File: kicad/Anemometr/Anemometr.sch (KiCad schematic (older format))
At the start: 157 parts, among them J10 +Z3, J11 -Z3, J12 +Z4, J13 -Z4, J14 SWD, J15 SWC, J16 Z4, J17 Z4, J18 1 TxD+, J19 2 TxD-, J2 Conn_01x01_Female, J20 3 RxD+, J21 4, J22 5, J23 6 RxD-, J24 7, J25 8, J26 Z4, J27 Z4, J28 Z4, J29 Z4, J3 RST, J30 Z4, J31 Z4, J32 Z4, J33 Z4, J34 Z4, J35 Z4, J4 TxD, J5 RxD, J6 +Z1, J7 -Z1, J8 +Z2, J9 -Z2, U1 TS5A3166DBVR, U10 MCP1700-3002E, U2 LMV7239, U3 TS5A3166DBVR, U4 TS5A3166DBVR, U5 STM32F103C8Tx, U6 TS5A3166DBVR, U7 LM2734Y, U8 MCP1700-5002E, U9 MCP1700-3002E, Y1 8MHz, Y2 25MHz

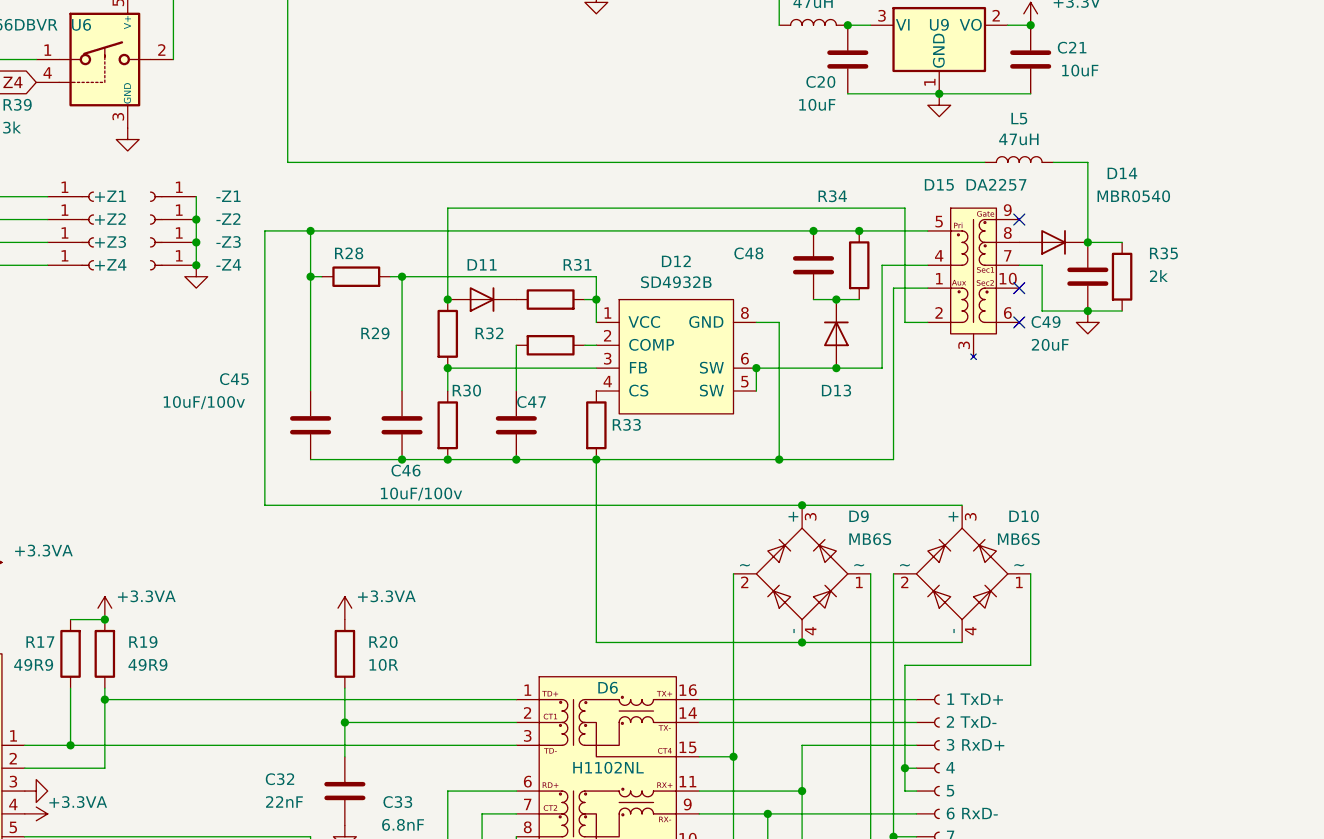
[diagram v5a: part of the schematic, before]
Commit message: изменено:      kicad/Anemometr/Anemometr-cache.lib 	изменено:      kicad/Anemometr/Anemometr.kicad_pcb 	изменено:      kicad/Anemometr/Anemometr.kicad_pcb-bak 	изменено:      kicad/Anemometr/Anemometr.sch 	изменено:      kicad/Anemometr/Anemometr.sch-bak 	изменено:      kicad/Anemometr/fp-info-cache
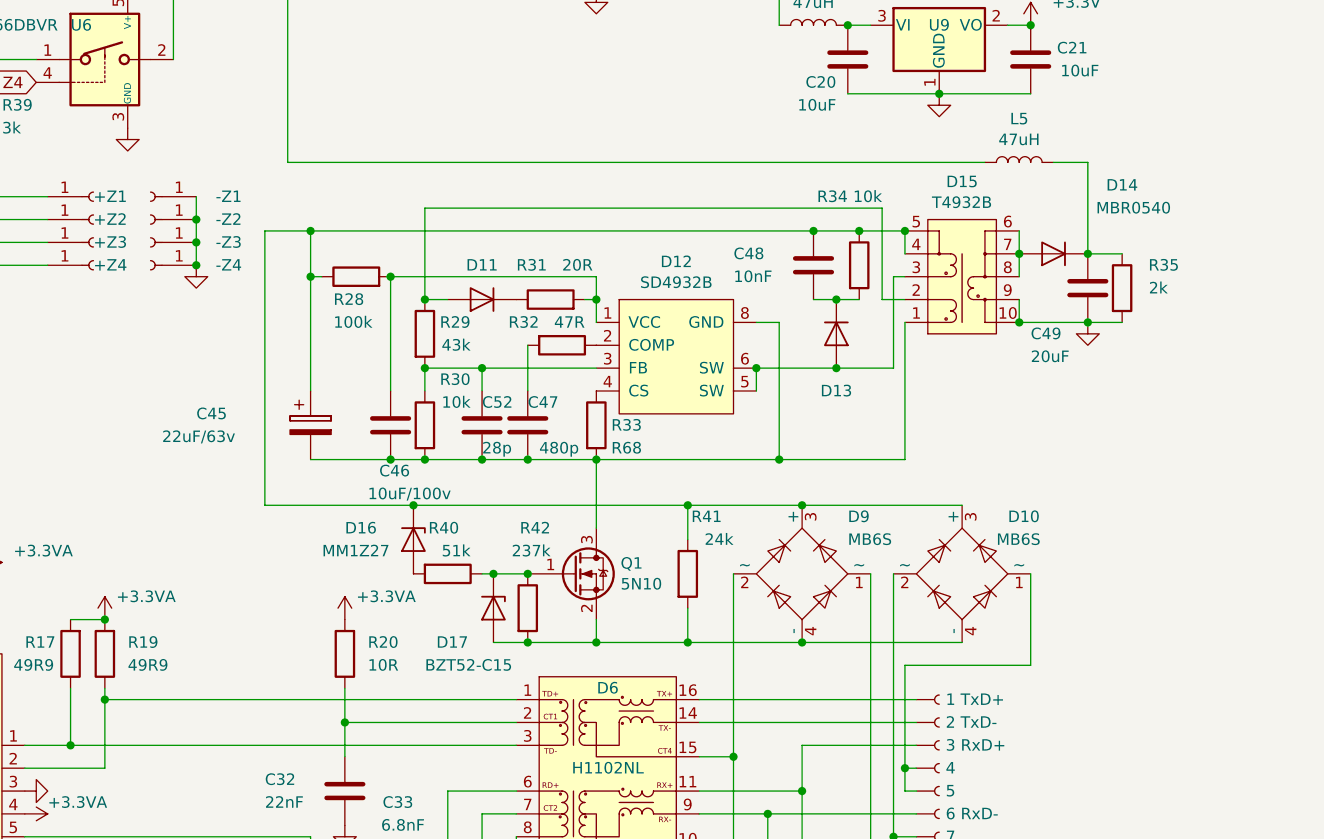
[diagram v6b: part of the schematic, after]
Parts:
- removed C45: 10uF/100v, Capacitor_SMD:C_0805_2012Metric, symbol Device:C
- removed D15: DA2257, My-library:DA2257, symbol Anemometr-rescue:DA2257-My_Library
- added C45: 22uF/63v, Capacitor_SMD:CP_Elec_6.3x7.7, symbol Device:CP
- added C52: 28p, Capacitor_SMD:C_0603_1608Metric, symbol Device:C
- added D15: T4932B, My-library:DA2257, symbol My_Library:T4932B
- added D16: MM1Z27, Diode_SMD:D_SOD-123, symbol Device:D_Zener
- added D17: BZT52-C15, Diode_SMD:D_SOD-123, symbol Device:D_Zener
- added Q1: 5N10, Package_TO_SOT_SMD:SOT-23, symbol Device:Q_NMOS_GSD
- added R40: 51k, Resistor_SMD:R_0603_1608Metric, symbol Device:R
- added R41: 24k, Resistor_SMD:R_0603_1608Metric, symbol Device:R
- added R42: 237k, Resistor_SMD:R_0603_1608Metric, symbol Device:R
- C47: value 6.8nF -> 480p
- C48: value 6.8nF -> 10nF
- R28: value 150R -> 100k
- R29: value 150R -> 43k
- R30, R34: value 150R -> 10k
- R31: value 150R -> 20R
- R32: value 150R -> 47R
- R33: value 150R -> R68
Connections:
- net GND: now also D15.10, D15.9
- net at C46.2, C47.2, D12.8 (GND)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: now also C45.2, C52.2, D15.1, Q1.3 (D); no longer D10.4 (-), D9.4 (-)
- net at D11.2 (A), R29.1: now also D15.2
- net at D12.5 (SW), D12.6 (SW), D13.2 (A): now also D15.3
- net at C48.1, D10.3 (+), D9.3 (+)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: now also C45.1, D15.4, D15.5, D16.1 (K), R41.1
- net at D14.2 (A): now also D15.6, D15.7, D15.8
- net at D12.3 (FB), R29.2, R30.1: now also C52.1
- new net: D17.1 (K), Q1.1 (G), R40.1, R42.1
- new net: D10.4 (-), D17.2 (A), D9.4 (-), Q1.2 (S), R41.2, R42.2
- new net: D16.2 (A), R40.2
- no-connect marks 32 -> 29
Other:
- moved on the sheet: C46, C47, C49, D14, R29, R30, R32, R35

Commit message: изменено:      kicad/Anemometr/Anemometr.kicad_pcb 	изменено:      kicad/Anemometr/Anemometr.kicad_pcb-bak 	изменено:      kicad/Anemometr/Anemometr.sch 	изменено:      kicad/Anemometr/Anemometr.sch-bak 	изменено:      kicad/Anemometr/fp-info-cache
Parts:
- removed C49: 20uF, Capacitor_SMD:C_1210_3225Metric, symbol Device:C
- removed R22: 75R, Resistor_SMD:R_0402_1005Metric, symbol Device:R
- added C49: 220uF, Capacitor_Tantalum_SMD:CP_EIA-7343-15_Kemet-W, symbol Device:CP
- added D18, D19: LED, LED_SMD:LED_0603_1608Metric, symbol Device:LED
- added J1: +5.5v, My-library:SMD-CONN, symbol Connector:Conn_01x01_Female
- added R43: 4.7k, Resistor_SMD:R_0603_1608Metric, symbol Device:R
- added R44: 2k, Resistor_SMD:R_0603_1608Metric, symbol Device:R
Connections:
- net GND: now also C49.2, D18.1 (K), D19.1 (K)
- net at C22.2, D2.2 (A), L5.1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: now also R43.2
- net at C17.2, L1.2, L2.1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: now also J1.1 (Pin_1), R44.1
- net at D6.11, J20.1: now also R23.2; no longer R24.2
- net at D6.9, J23.1: now also R24.2; no longer R23.2
- net at Q1.1 (G), R40.1, R42.1: now also D17.2 (A); no longer D17.1 (K)
- net at D10.4 (-), D9.4 (-), Q1.2 (S)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: now also D17.1 (K); no longer D17.2 (A)
- net at D14.1 (K), L5.2, R35.1: now also C49.1
- new net: D18.2 (A), R43.1
- new net: D19.2 (A), R44.2
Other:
- moved on the sheet: R23, R24, R41
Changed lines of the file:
@@
 U 1 1 61DA4E2B
 P 9900 3800
-F 0 "R12" V 10200 3800 50  0000 R CNN
-F 1 "100k" V 10100 3800 50  0000 R CNN
+F 0 "R12" V 10200 3600 50  0000 R CNN
+F 1 "100k" V 10100 3600 50  0000 R CNN
 F 2 "Resistor_SMD:R_0805_2012Metric" V 9830 3800 50  0001 C CNN
 F 3 "~" H 9900 3800 50  0001 C CNN
@@
 $EndComp
 $Comp
-L Device:R R21
-U 1 1 61FFF702
-P 9950 8100
-F 0 "R21" H 10150 8050 50  0000 R CNN
-F 1 "75R" H 10150 8150 50  0000 R CNN
-F 2 "Resistor_SMD:R_0402_1005Metric" V 9880 8100 50  0001 C CNN
-F 3 "~" H 9950 8100 50  0001 C CNN
-	1    9950 8100
-	-1   0    0    1
-$EndComp
-$Comp
-L Device:R R22
-U 1 1 61FFFDD0
-P 10100 8100
-F 0 "R22" H 10100 8450 50  0000 R CNN
-F 1 "75R" H 10100 8550 50  0000 R CNN
-F 2 "Resistor_SMD:R_0402_1005Metric" V 10030 8100 50  0001 C CNN
-F 3 "~" H 10100 8100 50  0001 C CNN
-	1    10100 8100
-	-1   0    0    1
-$EndComp
-$Comp
-L Device:C C35
-U 1 1 62000309
-P 9950 8400
-F 0 "C35" H 10150 8350 50  0000 L CNN
-F 1 "4.7nF/2kV" H 10100 8450 50  0000 L CNN
-F 2 "Capacitor_SMD:C_0805_2012Metric" H 9988 8250 50  0001 C CNN
-F 3 "~" H 9950 8400 50  0001 C CNN
-	1    9950 8400
-	-1   0    0    1
-$EndComp
-$Comp
-L power:GND #PWR048
-U 1 1 6200A94F
-P 9950 8550
-F 0 "#PWR048" H 9950 8300 50  0001 C CNN
-F 1 "GND" H 9955 8377 50  0001 C CNN
-F 2 "" H 9950 8550 50  0001 C CNN
-F 3 "" H 9950 8550 50  0001 C CNN
-	1    9950 8550
-	1    0    0    -1
-$EndComp
-$Comp
 L Anemometr-rescue:Conn-My_Library J18
 U 1 1 6201FB36
@@
 	9950 7350 10900 7350
 Wire Wire Line
-	9950 7650 10400 7650
-Wire Wire Line
-	9950 7500 10100 7500
-$Comp
-L Device:R R23
-U 1 1 62116815
-P 10250 8100
-F 0 "R23" H 10200 8450 50  0000 R CNN
-F 1 "150R" H 10200 8550 50  0000 R CNN
-F 2 "Resistor_SMD:R_0402_1005Metric" V 10180 8100 50  0001 C CNN
-F 3 "~" H 10250 8100 50  0001 C CNN
-	1    10250 8100
-	-1   0    0    1
-$EndComp
-$Comp
-L Device:R R24
-U 1 1 6211700D
-P 10400 8100
-F 0 "R24" H 10300 8050 50  0000 R CNN
-F 1 "150R" H 10300 8150 50  0000 R CNN
-F 2 "Resistor_SMD:R_0402_1005Metric" V 10330 8100 50  0001 C CNN
-F 3 "~" H 10400 8100 50  0001 C CNN
-	1    10400 8100
-	-1   0    0    1
-$EndComp
-Wire Wire Line
-	10400 7650 10400 7450
-Wire Wire Line
-	10400 7450 10900 7450
+	9950 7650 10100 7650
 $Comp
 L Device:LED D8
@@
 Connection ~ 10800 7850
 Wire Wire Line
-	10100 7500 10100 6700
-Wire Wire Line
 	10700 6700 10700 7900
 Wire Wire Line
@@
 $EndComp
 $Comp
-L Device:C C49
-U 1 1 629FDA3F
-P 11650 5450
-F 0 "C49" H 11400 5250 50  0000 L CNN
-F 1 "20uF" H 11400 5150 50  0000 L CNN
-F 2 "Capacitor_SMD:C_1210_3225Metric" H 11688 5300 50  0001 C CNN
-F 3 "~" H 11650 5450 50  0001 C CNN
-	1    11650 5450
-	1    0    0    -1
-$EndComp
-$Comp
 L Device:R R35
 U 1 1 629FDF7E
@@
 	9700 1800 9700 2000
 Wire Wire Line
-	9950 7950 9950 7900
-Connection ~ 9950 7900
-Wire Wire Line
-	10100 7950 10100 7500
-Connection ~ 10100 7500
-Wire Wire Line
-	9950 7750 10250 7750
-Wire Wire Line
-	10250 7950 10250 7750
-Connection ~ 10250 7750
-Wire Wire Line
-	10250 7750 10900 7750
-Wire Wire Line
-	10400 7950 10400 7650
-Connection ~ 10400 7650
-Wire Wire Line
-	9950 8250 10100 8250
-Connection ~ 9950 8250
-Connection ~ 10100 8250
-Wire Wire Line
-	10100 8250 10250 8250
-Connection ~ 10250 8250
-Wire Wire Line
-	10250 8250 10400 8250
-Wire Wire Line
 	8750 5900 8750 5800
 Wire Wire Line
-	9500 7000 9900 7000
+	9500 7000 9700 7000
 Wire Wire Line
 	8150 4900 11200 4900
@@
 	8150 3150 8550 3150
 Wire Wire Line
-	8150 3150 8150 4900
+	8150 3150 8150 4300
 Connection ~ 8550 3150
 $Comp
@@
 U 1 1 61F86A88
 P 9400 6700
-F 0 "Q1" H 9606 6746 50  0000 L CNN
-F 1 "5N10" H 9606 6655 50  0000 L CNN
+F 0 "Q1" H 9450 6350 50  0000 L CNN
+F 1 "5N10" H 9600 6350 50  0000 L CNN
 F 2 "Package_TO_SOT_SMD:SOT-23" H 9600 6800 50  0001 C CNN
 F 3 "~" H 9400 6700 50  0001 C CNN
@@
 L Device:R R41
 U 1 1 6207208D
-P 9900 6700
-F 0 "R41" H 10050 6950 50  0000 R CNN
-F 1 "24k" H 10100 6850 50  0000 R CNN
-F 2 "Resistor_SMD:R_0603_1608Metric" V 9830 6700 50  0001 C CNN
-F 3 "~" H 9900 6700 50  0001 C CNN
-	1    9900 6700
-	1    0    0    -1
-$EndComp
-Wire Wire Line
-	9900 6550 9900 6400
-Connection ~ 9900 6400
-Wire Wire Line
-	9900 6400 10400 6400
-Wire Wire Line
-	9900 6850 9900 7000
-Connection ~ 9900 7000
-Wire Wire Line
-	9900 7000 10400 7000
+P 9700 6700
+F 0 "R41" H 9850 6950 50  0000 R CNN
+F 1 "24k" H 9900 6850 50  0000 R CNN
+F 2 "Resistor_SMD:R_0603_1608Metric" V 9630 6700 50  0001 C CNN
+F 3 "~" H 9700 6700 50  0001 C CNN
+	1    9700 6700
+	1    0    0    -1
+$EndComp
 $Comp
 L Device:D_Zener D16
@@
 Connection ~ 8700 6400
 Wire Wire Line
-	8700 6400 9900 6400
+	8700 6400 9700 6400
 Wire Wire Line
 	9000 6700 9050 6700
@@
 U 1 1 620B088D
 P 9050 6850
-F 0 "D17" V 9200 6600 50  0000 L CNN
-F 1 "BZT52-C15" V 9300 6550 50  0000 L CNN
+F 0 "D17" V 8950 6900 50  0000 L CNN
+F 1 "BZT52-C15" V 8850 6750 50  0000 L CNN
 F 2 "Diode_SMD:D_SOD-123" H 9050 6850 50  0001 C CNN
 F 3 "~" H 9050 6850 50  0001 C CNN
 	1    9050 6850
-	0    1    1    0
+	0    -1   -1   0
 $EndComp
 Connection ~ 9050 6700
@@
 	10800 5400 10850 5400
 Wire Wire Line
-	10850 5600 10850 6200
-Wire Wire Line
 	10300 6200 10850 6200
 Wire Wire Line
@@
 Wire Wire Line
 	11650 4900 11650 5300
+$Comp
+L Device:R R43
+U 1 1 620F34A0
+P 8300 4300
+F 0 "R43" V 8100 4350 50  0000 R CNN
+F 1 "4.7k" V 8200 4350 50  0000 R CNN
+F 2 "Resistor_SMD:R_0603_1608Metric" V 8230 4300 50  0001 C CNN
+F 3 "~" H 8300 4300 50  0001 C CNN
+	1    8300 4300
+	0    1    1    0
+$EndComp
+Connection ~ 8150 4300
+Wire Wire Line
+	8150 4300 8150 4900
+$Comp
+L Device:LED D18
+U 1 1 620F6B14
+P 8450 4450
+F 0 "D18" V 8550 4300 50  0000 R CNN
+F 1 "LED" V 8398 4333 50  0001 R CNN
+F 2 "LED_SMD:LED_0603_1608Metric" H 8450 4450 50  0001 C CNN
+F 3 "~" H 8450 4450 50  0001 C CNN
+	1    8450 4450
+	0    -1   -1   0
+$EndComp
+$Comp
+L power:GND #PWR052
+U 1 1 620FBFC5
+P 8450 4600
+F 0 "#PWR052" H 8450 4350 50  0001 C CNN
+F 1 "GND" H 8455 4427 50  0001 C CNN
+F 2 "" H 8450 4600 50  0001 C CNN
+F 3 "" H 8450 4600 50  0001 C CNN
+	1    8450 4600
+	1    0    0    -1
+$EndComp
+$Comp
+L Connector:Conn_01x01_Female J1
+U 1 1 62105095
+P 10300 2900
+F 0 "J1" H 9800 2900 50  0001 C CNN
+F 1 "+5.5v" V 10400 2800 50  0000 L CNN
+F 2 "My-library:SMD-CONN" H 10300 2900 50  0001 C CNN
+F 3 "~" H 10300 2900 50  0001 C CNN
+	1    10300 2900
+	0    -1   -1   0
+$EndComp
+$Comp
+L Device:R R44
+U 1 1 621C9B5C
+P 10150 3100
+F 0 "R44" V 9950 3150 50  0000 R CNN
+F 1 "2k" V 10050 3150 50  0000 R CNN
+F 2 "Resistor_SMD:R_0603_1608Metric" V 10080 3100 50  0001 C CNN
+F 3 "~" H 10150 3100 50  0001 C CNN
+	1    10150 3100
+	0    1    1    0
+$EndComp
+$Comp
+L Device:LED D19
+U 1 1 621CB231
+P 10000 3250
+F 0 "D19" V 10000 3150 50  0000 R CNN
+F 1 "LED" V 9948 3133 50  0001 R CNN
+F 2 "LED_SMD:LED_0603_1608Metric" H 10000 3250 50  0001 C CNN
+F 3 "~" H 10000 3250 50  0001 C CNN
+	1    10000 3250
+	0    -1   -1   0
+$EndComp
+Connection ~ 10300 3100
+$Comp
+L power:GND #PWR061
+U 1 1 6225054D
+P 10000 3400
+F 0 "#PWR061" H 10000 3150 50  0001 C CNN
+F 1 "GND" H 10005 3227 50  0001 C CNN
+F 2 "" H 10000 3400 50  0001 C CNN
+F 3 "" H 10000 3400 50  0001 C CNN
+	1    10000 3400
+	1    0    0    -1
+$EndComp
+$Comp
+L Device:CP C49
+U 1 1 62482746
+P 11650 5450
+F 0 "C49" H 11350 5200 50  0000 L CNN
+F 1 "220uF" H 11350 5100 50  0000 L CNN
+F 2 "Capacitor_Tantalum_SMD:CP_EIA-7343-15_Kemet-W" H 11688 5300 50  0001 C CNN
+F 3 "~" H 11650 5450 50  0001 C CNN
+	1    11650 5450
+	1    0    0    -1
+$EndComp
+Wire Wire Line
+	9700 6850 9700 7000
+Connection ~ 9700 7000
+Wire Wire Line
+	9700 6550 9700 6400
+Connection ~ 9700 6400
+Wire Wire Line
+	9700 6400 10400 6400
+Wire Wire Line
+	9700 7000 10400 7000
+Wire Wire Line
+	9950 7500 10000 7500
+Wire Wire Line
+	10000 7500 10000 6700
+Wire Wire Line
+	10000 6700 10100 6700
+Wire Wire Line
+	10100 7650 10100 7450
+Wire Wire Line
+	10100 7450 10900 7450
+Wire Wire Line
+	10850 5600 10850 6200
+$Comp
+L power:GND #PWR048
+U 1 1 6200A94F
+P 9950 8550
+F 0 "#PWR048" H 9950 8300 50  0001 C CNN
+F 1 "GND" H 9955 8377 50  0001 C CNN
+F 2 "" H 9950 8550 50  0001 C CNN
+F 3 "" H 9950 8550 50  0001 C CNN
+	1    9950 8550
+	1    0    0    -1
+$EndComp
+$Comp
+L Device:C C35
+U 1 1 62000309
+P 9950 8400
+F 0 "C35" H 10150 8350 50  0000 L CNN
+F 1 "4.7nF/2kV" H 10100 8450 50  0000 L CNN
+F 2 "Capacitor_SMD:C_0805_2012Metric" H 9988 8250 50  0001 C CNN
+F 3 "~" H 9950 8400 50  0001 C CNN
+	1    9950 8400
+	-1   0    0    1
+$EndComp
+Wire Wire Line
+	10250 7750 10900 7750
+Wire Wire Line
+	9950 7750 10250 7750
+Connection ~ 10250 7750
+Wire Wire Line
+	10250 7950 10250 7750
+Connection ~ 9950 7900
+Wire Wire Line
+	9950 7950 9950 7900
+Connection ~ 10100 7650
+Wire Wire Line
+	10100 7950 10100 7650
+Connection ~ 9950 8250
+$Comp
+L Device:R R21
+U 1 1 61FFF702
+P 9950 8100
+F 0 "R21" H 10150 8050 50  0000 R CNN
+F 1 "75R" H 10150 8150 50  0000 R CNN
+F 2 "Resistor_SMD:R_0402_1005Metric" V 9880 8100 50  0001 C CNN
+F 3 "~" H 9950 8100 50  0001 C CNN
+	1    9950 8100
+	-1   0    0    1
+$EndComp
+Wire Wire Line
+	10100 8250 10250 8250
+Wire Wire Line
+	9950 8250 10100 8250
+Connection ~ 10100 8250
+$Comp
+L Device:R R23
+U 1 1 62116815
+P 10100 8100
+F 0 "R23" H 10050 8450 50  0000 R CNN
+F 1 "150R" H 10050 8550 50  0000 R CNN
+F 2 "Resistor_SMD:R_0402_1005Metric" V 10030 8100 50  0001 C CNN
+F 3 "~" H 10100 8100 50  0001 C CNN
+	1    10100 8100
+	-1   0    0    1
+$EndComp
+$Comp
+L Device:R R24
+U 1 1 6211700D
+P 10250 8100
+F 0 "R24" H 10150 8050 50  0000 R CNN
+F 1 "150R" H 10150 8150 50  0000 R CNN
+F 2 "Resistor_SMD:R_0402_1005Metric" V 10180 8100 50  0001 C CNN
+F 3 "~" H 10250 8100 50  0001 C CNN
+	1    10250 8100
+	-1   0    0    1
+$EndComp
 $EndSCHEMATC

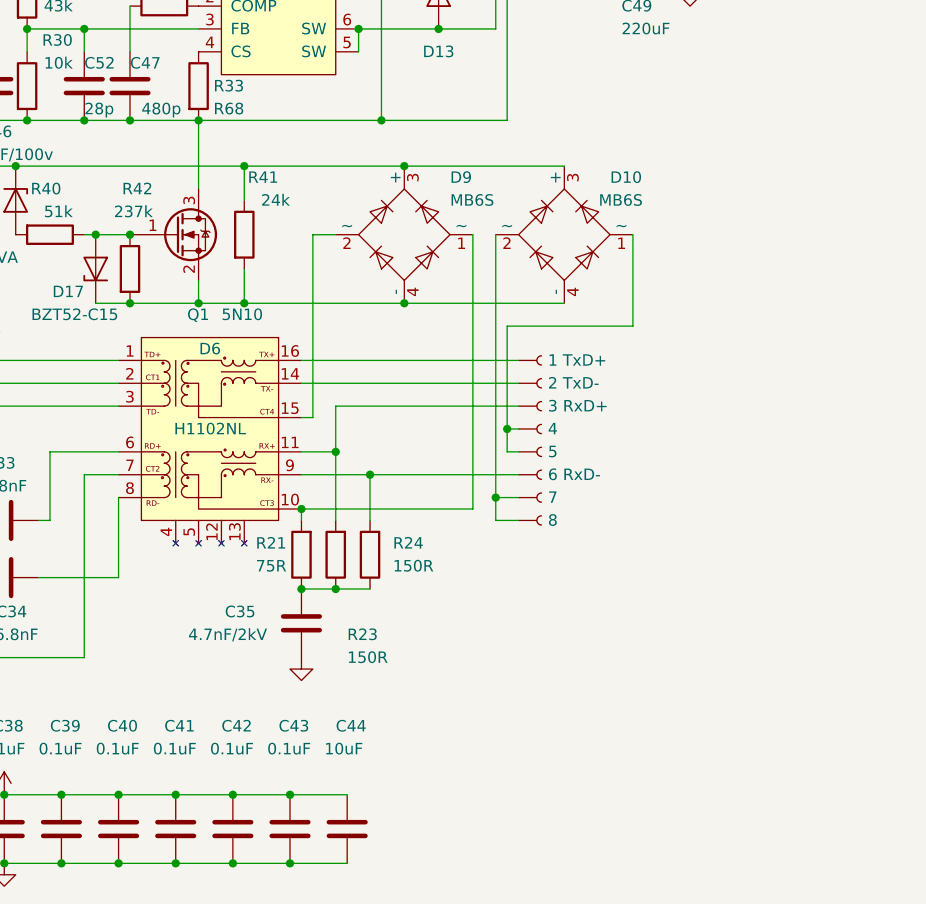
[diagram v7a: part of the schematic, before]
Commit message: изменено:      kicad/Anemometr/Anemometr.sch 	изменено:      kicad/Anemometr/Anemometr.sch-bak
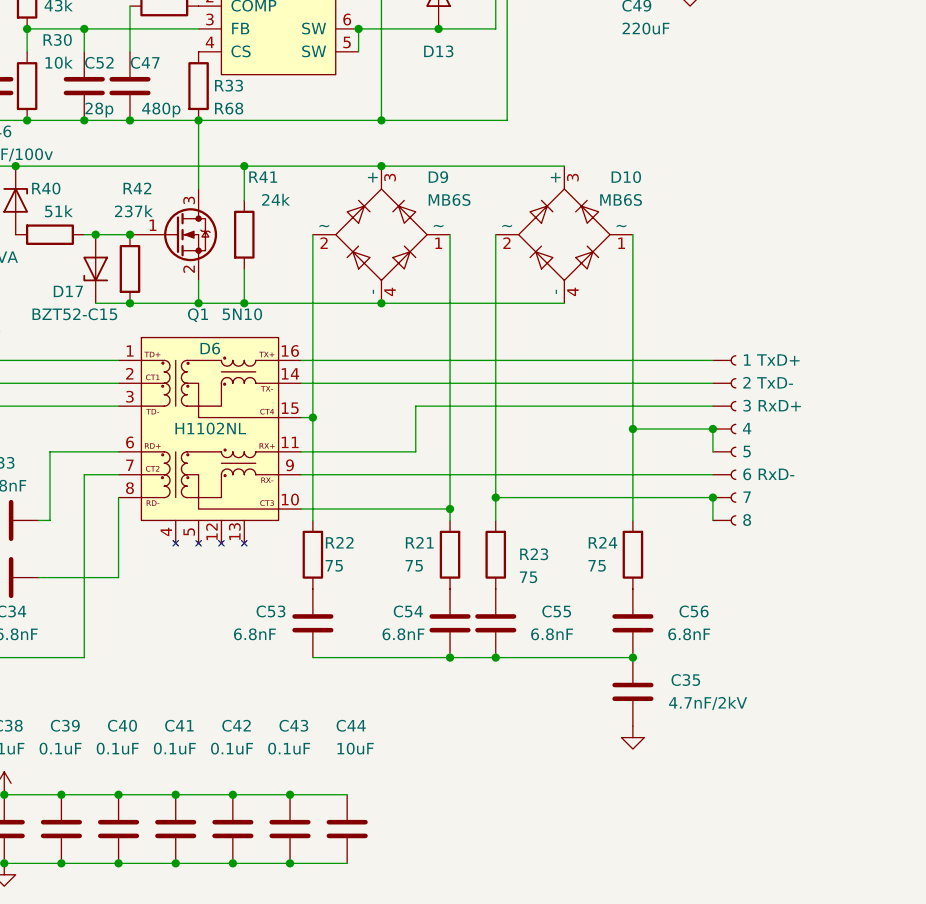
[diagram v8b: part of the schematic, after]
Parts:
- added C53, C54, C55, C56: 6.8nF, Capacitor_SMD:C_0603_1608Metric, symbol Device:C
- added R22: 75, Resistor_SMD:R_0402_1005Metric, symbol Device:R
- R21: value 75R -> 75
- R23, R24: value 150R -> 75
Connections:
- net at D6.11, J20.1: no longer R23.2
- net at D6.15, D9.2 (~~): now also R22.2
- net at D6.9, J23.1: no longer R24.2
- net at D10.1 (~~), J21.1, J22.1: now also R24.2
- net at D10.2 (~~), J24.1, J25.1: now also R23.2
- new net: C54.1, R21.1
- new net: C35.2, C53.2, C54.2, C55.2, C56.2
- new net: C53.1, R22.1
- new net: C55.1, R23.1
- new net: C56.1, R24.1
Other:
- moved on the sheet: C35, D9, R21, R23, R24
